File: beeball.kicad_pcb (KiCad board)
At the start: 2 copper layers, 91.4 x 58.4 mm, 13 parts, among them SW1 SW_Push, SW2 SW_Push, SW3 SW_Push, U1 SeeeduinoXIAO, U2 PMW3360DM-T2QU, U3 TLV70019_SOT23-5

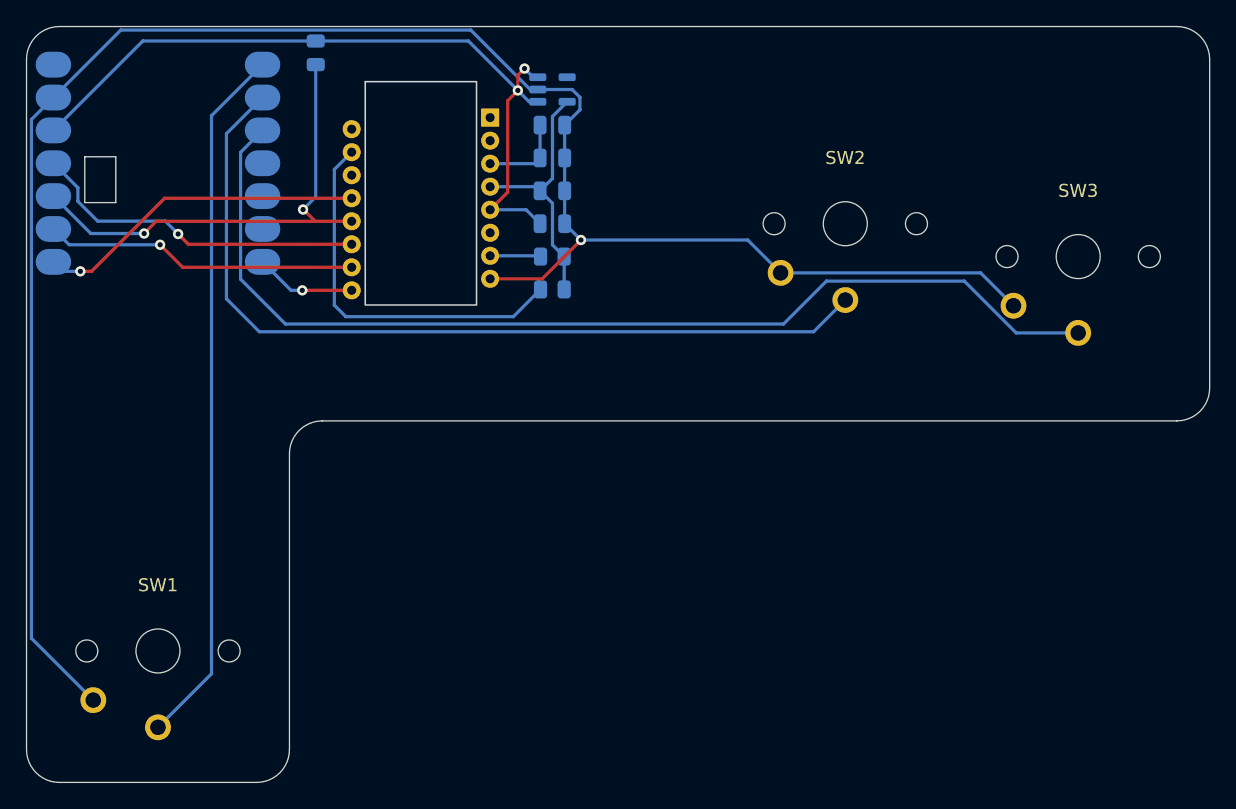
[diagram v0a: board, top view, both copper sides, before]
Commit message: Fix battery cutout, change M2 mounting holes to M3, change Choc switch footprint to MX+Choc+Alps footprint
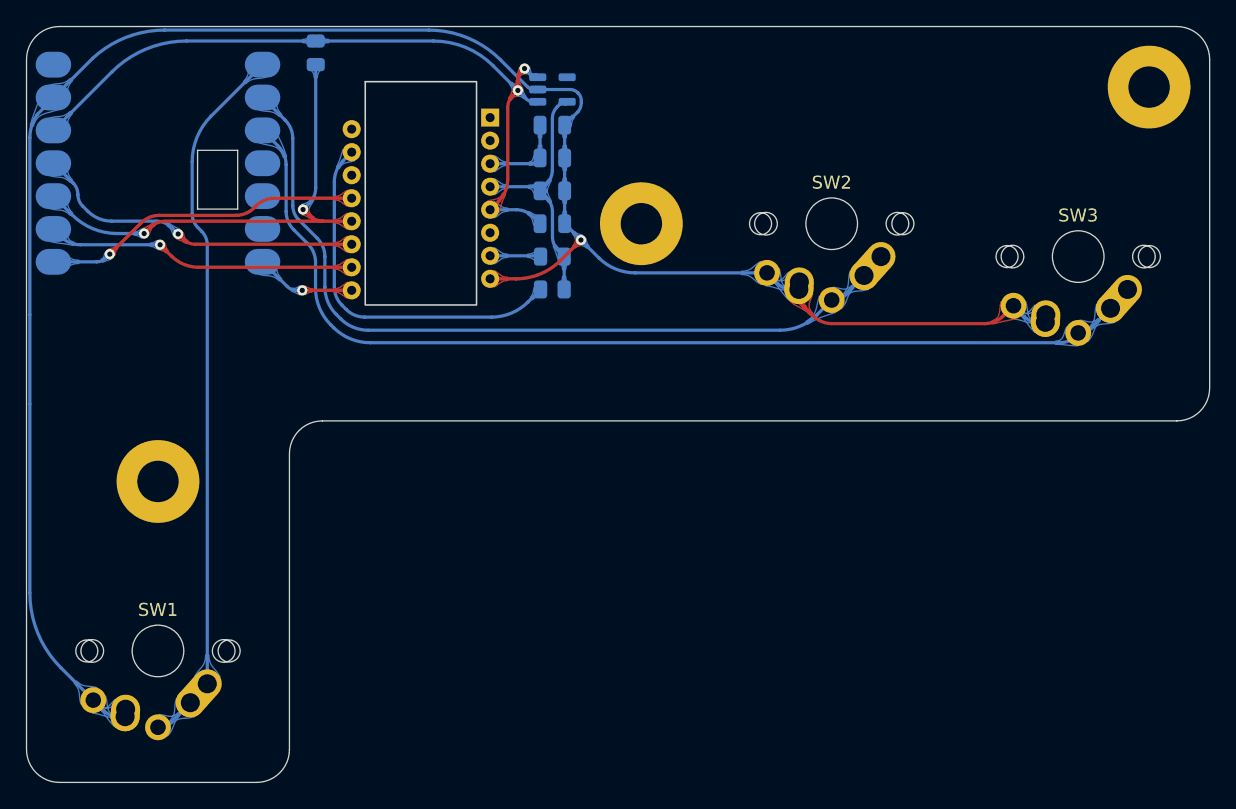
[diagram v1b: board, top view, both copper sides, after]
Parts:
- added H1: MountingHole_Pad, MountingHole:MountingHole_3.2mm_M3_Pad, B.Cu at (104.1, 101.2)
- added H2: MountingHole_Pad, MountingHole:MountingHole_3.2mm_M3_Pad, B.Cu at (141.5, 81.3)
- added H3: MountingHole_Pad, MountingHole:MountingHole_3.2mm_M3_Pad, B.Cu at (180.7, 70.7)
- SW1, SW2, SW3: footprint Project Footprints:Kailh-PG1350-1u -> Project Footprints:MX-Alps-Choc-1U
- moved SW2 1.05 mm to (156.2, 81.3)
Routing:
- net GND: track 150.1 -> 156.6 mm
- net sw2: track 66.6 -> 61.4 mm
- net sw3: track 81.4 -> 78.4 mm
- net sw1: track 54.6 -> 53.4 mm
- net VCC: track 59.9 -> 58.8 mm
- net ncs: track 25.7 -> 24.8 mm
- net Net-(R1-Pad2): track 29.6 -> 28.7 mm
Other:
- outline, holes or cut-outs redrawn

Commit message: Fix Xiao battery cutout alignment
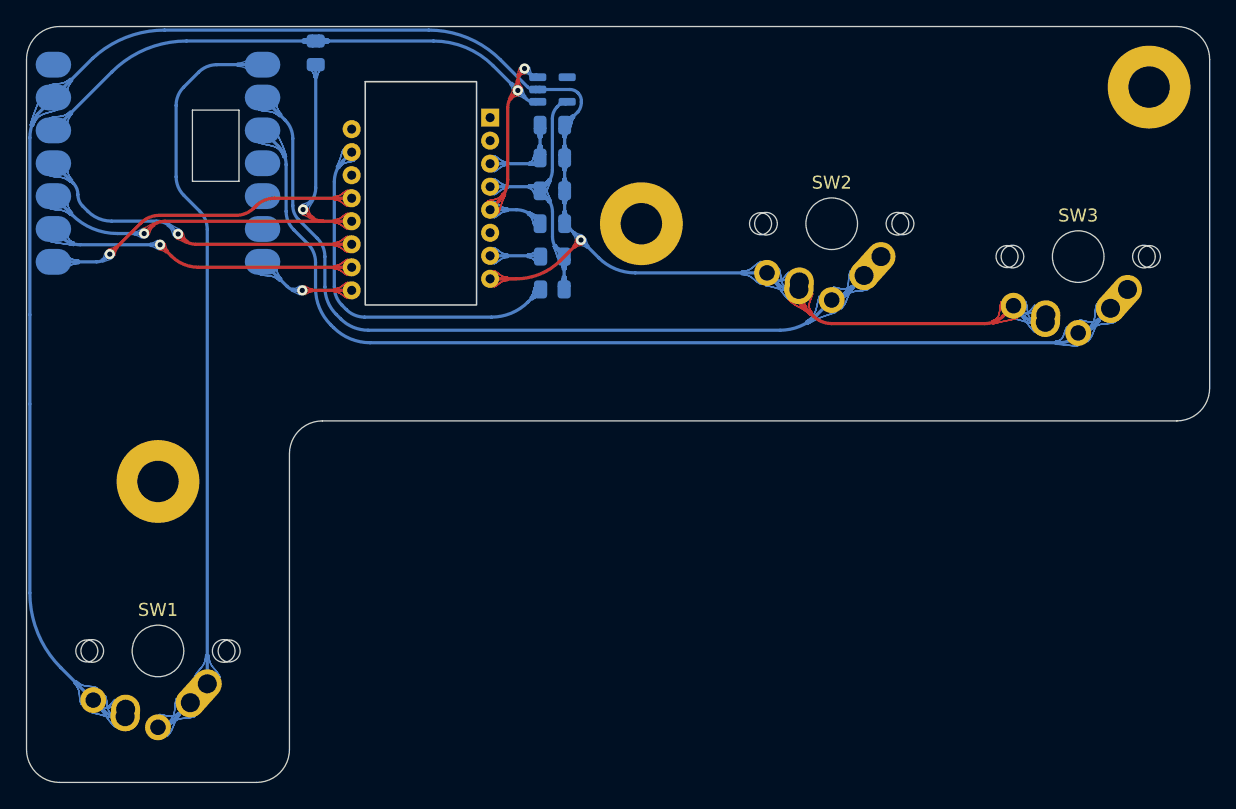
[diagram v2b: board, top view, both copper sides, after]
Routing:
- net sw1: track 53.4 -> 57.0 mm
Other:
- outline, holes or cut-outs redrawn
